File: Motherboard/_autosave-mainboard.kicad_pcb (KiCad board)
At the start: 4 copper layers, 45.2 x 36 mm, 53 parts, among them IC1 BMX160, J1 Conn_01x01, J2 10118194-0001LF, J28 Conn_01x01, J29 Conn_01x01, J3 Micro_SD_Card, J30 Conn_01x01, J4 xf2m-2415-1a, J5 XF2M-1015-1A, J6 U.FL-R-SMT-1, J7 U.FL-R-SMT-1, J8 Conn_01x01, J9 XF2M36151A, SW1 KMR231NG LFS, U1 RFM95W-915S2, U2 ATSAMD51G_TQFN48, U3 DRV8848, U4 TPS82740BSIPR, U5 DRV8848, U6 MAX708RESA-T, U8 RFM95W-915S2

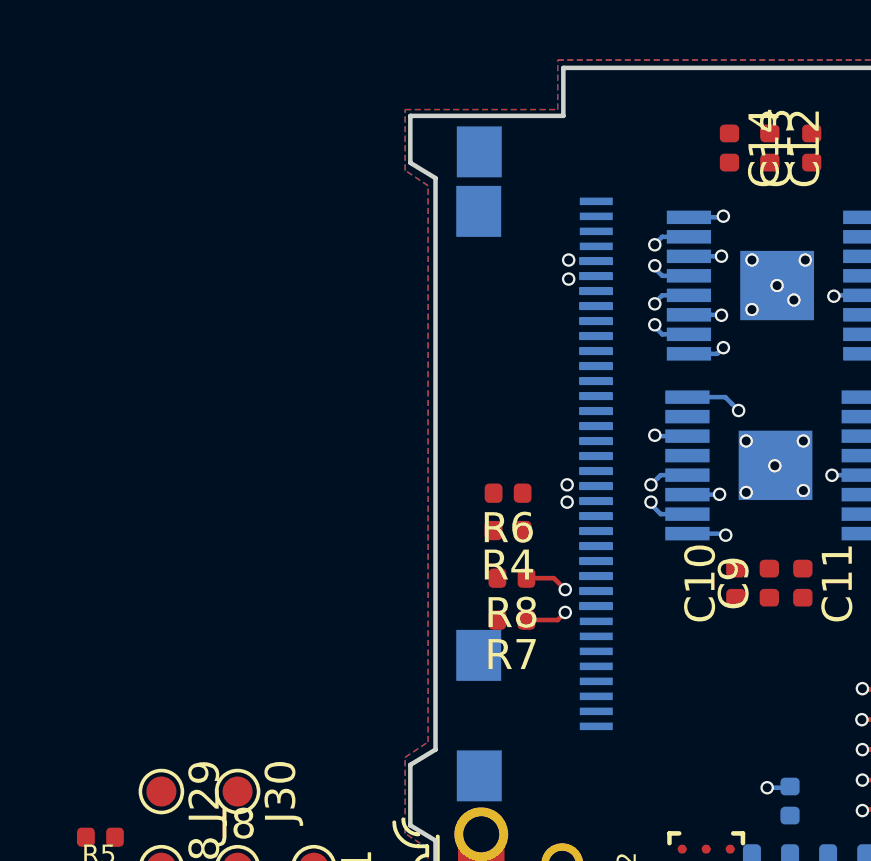
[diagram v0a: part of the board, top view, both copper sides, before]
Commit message: putting matching coils in series
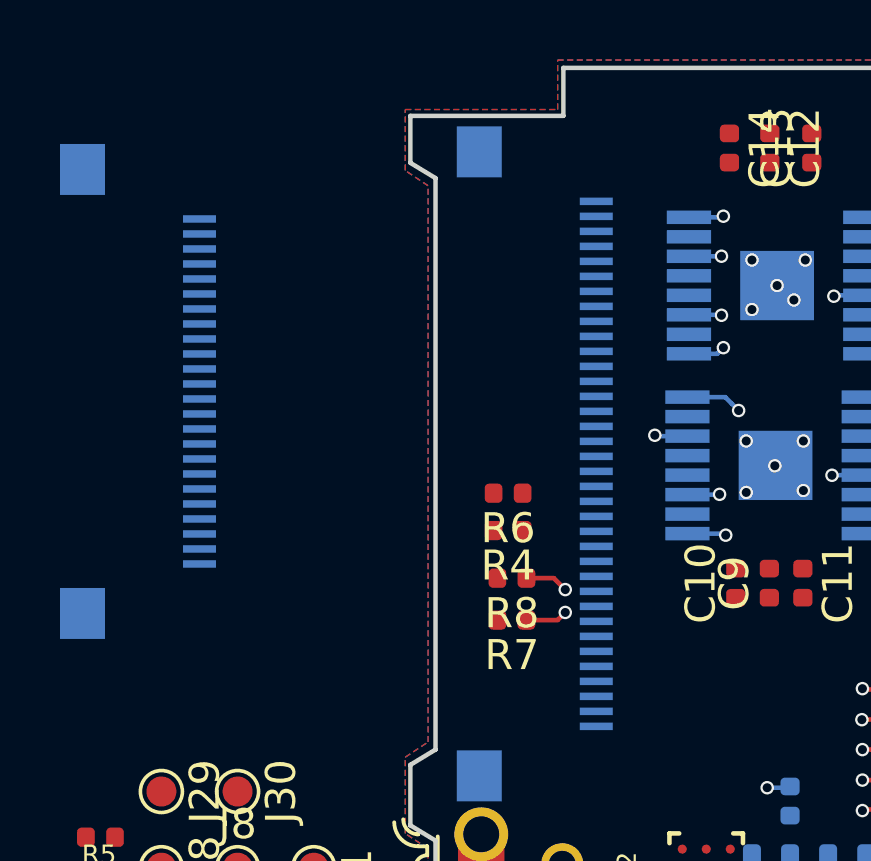
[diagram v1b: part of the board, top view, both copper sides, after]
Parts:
- moved J4 13.3 mm to (69.6, 84.3)
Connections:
- net Net-(J9-Pad29) renamed COIL4N
- net Net-(J9-Pad30) renamed COIL4P
- J4 pad 10: COIL3P -> Net-(J4-Pad10)
- J4 pad 12: COIL3N -> Net-(J4-Pad12)
- J4 pad 3: COIL1P -> Net-(J4-Pad3)
- J4 pad 4: COIL1N -> Net-(J4-Pad4)
- J4 pad 6: COIL2P -> Net-(J4-Pad6)
- J4 pad 8: COIL2N -> Net-(J4-Pad8)
- J9 pad 31: Net-(J9-Pad31) -> COIL3N
- J9 pad 32: Net-(J9-Pad32) -> COIL3P
- J9 pad 33: Net-(J9-Pad33) -> COIL2P
- J9 pad 34: Net-(J9-Pad34) -> COIL2N
- J9 pad 35: Net-(J9-Pad35) -> COIL1N
- J9 pad 36: Net-(J9-Pad36) -> COIL1P
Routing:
- net MOX_1: track 4.55 -> 0.00 mm, vias 1 -> 0
- net MOX_2: track 4.49 -> 0.00 mm, vias 1 -> 0
- net MOZ_2: track 4.49 -> 0.00 mm, vias 2 -> 0
- net MOY_1: track 4.45 -> 0.00 mm, vias 2 -> 0
- net MOZ_1: track 4.34 -> 0.00 mm, vias 2 -> 0
- net MOY_2: track 4.25 -> 0.00 mm, vias 2 -> 0
